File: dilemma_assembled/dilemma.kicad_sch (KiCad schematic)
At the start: 103 parts, among them J1 USB_C_Receptacle_USB2.0, J102 Serial, J103 Serial, J105 Conn_01x04_Female, J107 Conn_01x08_Female, J108 Conn_01x01_Female, J109 Conn_01x01_Female, J113 Cirque, J5 Conn_01x02, SW1 SW_Push, SW101 SW_Push, SW102 SW_Push, SW103 SW_Push, SW104 SW_Push, SW105 SW_Push, SW106 SW_Push, SW107 SW_Push, SW108 SW_Push, SW109 SW_Push, SW110 SW_SPST, SW111 SW_SPST, SW112 SW_Push, SW113 SW_Push, SW114 SW_Push, SW115 SW_Push, SW116 SW_Push, SW117 SW_Push, SW118 SW_Push, SW119 SW_Push, SW2 SW_Push, U1 RP2040, U2 GD25Q80CEIGR, U3 XC6210B332MR-G, Y1 Crystal_GND24

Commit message: add tooling holes, fancy M3 holes with vias
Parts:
- added H103, H109, H110: t, local-libraries:JLC_SMT_Assembly_Hole, symbol Mechanical:MountingHole_Pad
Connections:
- net GND: now also H103.1, H109.1, H110.1
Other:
- note added: "Assembly holes"
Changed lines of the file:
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@@
     (stroke (width 0) (type default) (color 0 0 0 0))
   )
+  (polyline (pts (xy 285.75 125.73) (xy 285.75 150.495))
+    (stroke (width 0) (type default) (color 0 0 0 0))
+  )
   (wire (pts (xy 267.97 137.16) (xy 256.54 137.16))
     (stroke (width 0) (type default) (color 0 0 0 0))
@@
     (stroke (width 0) (type default) (color 0 0 0 0))
   )
+  (polyline (pts (xy 312.42 150.495) (xy 285.75 150.495))
+    (stroke (width 0) (type default) (color 0 0 0 0))
+  )
   (wire (pts (xy 228.6 57.15) (xy 237.49 57.15))
     (stroke (width 0) (type default) (color 0 0 0 0))
@@
     (stroke (width 0) (type default) (color 0 0 0 0))
   )
+  (polyline (pts (xy 285.75 125.73) (xy 312.42 125.73))
+    (stroke (width 0) (type default) (color 0 0 0 0))
+  )
   (wire (pts (xy 90.17 228.6) (xy 93.98 228.6))
     (stroke (width 0) (type default) (color 0 0 0 0))
@@
     (stroke (width 0) (type default) (color 0 0 0 0))
   )
+  (polyline (pts (xy 312.42 125.73) (xy 312.42 150.495))
+    (stroke (width 0) (type default) (color 0 0 0 0))
+  )
   (wire (pts (xy 166.37 184.15) (xy 166.37 185.42))
     (stroke (width 0) (type default) (color 0 0 0 0))
@@
     (effects (font (size 1.778 1.778) (thickness 0.3556) bold) (justify left bottom))
   )
+  (text "Assembly holes" (at 307.34 125.73 180)
+    (effects (font (size 1.778 1.778) (thickness 0.3556) bold) (justify right bottom))
+  )
   (text "Serial" (at 249.555 165.735 0)
     (effects (font (size 1.778 1.778) (thickness 0.3556) bold) (justify left bottom))
@@
     (pin "2")
   )
+  (symbol (lib_id "power:GND") (at 306.07 135.89 0) (unit 1)
+    (in_bom yes) (on_board yes)
+    (property "Reference" "#PWR0116" (id 0) (at 306.07 142.24 0)
+      (effects (font (size 1.27 1.27)) hide)
+    )
+    (property "Value" "GND" (id 1) (at 305.914 142.8749 90)
+      (effects (font (size 1.27 1.27)) (justify left))
+    )
+    (property "Footprint" "" (id 2) (at 306.07 135.89 0)
+      (effects (font (size 1.27 1.27)) hide)
+    )
+    (property "Datasheet" "" (id 3) (at 306.07 135.89 0)
+      (effects (font (size 1.27 1.27)) hide)
+    )
+    (pin "1")
+  )
   (symbol (lib_id "Mechanical:MountingHole_Pad") (at 233.045 176.53 0) (unit 1)
     (in_bom yes) (on_board yes)
@@
     (pin "2")
   )
+  (symbol (lib_id "power:GND") (at 298.45 135.89 0) (unit 1)
+    (in_bom yes) (on_board yes)
+    (property "Reference" "#PWR0109" (id 0) (at 298.45 142.24 0)
+      (effects (font (size 1.27 1.27)) hide)
+    )
+    (property "Value" "GND" (id 1) (at 298.294 142.8749 90)
+      (effects (font (size 1.27 1.27)) (justify left))
+    )
+    (property "Footprint" "" (id 2) (at 298.45 135.89 0)
+      (effects (font (size 1.27 1.27)) hide)
+    )
+    (property "Datasheet" "" (id 3) (at 298.45 135.89 0)
+      (effects (font (size 1.27 1.27)) hide)
+    )
+    (pin "1")
+  )
   (symbol (lib_id "power:GND") (at 82.55 186.69 0) (unit 1)
     (in_bom yes) (on_board yes)
@@
     (pin "1")
   )
+  (symbol (lib_id "Mechanical:MountingHole_Pad") (at 306.07 133.35 0) (unit 1)
+    (in_bom yes) (on_board yes)
+    (property "Reference" "H110" (id 0) (at 304.8 128.27 0)
+      (effects (font (size 1.27 1.27)) (justify left))
+    )
+    (property "Value" "t" (id 1) (at 304.8 145.542 0)
+      (effects (font (size 1.27 1.27)) (justify left))
+    )
+    (property "Footprint" "local-libraries:JLC_SMT_Assembly_Hole" (id 2) (at 306.07 133.35 0)
+      (effects (font (size 1.27 1.27)) hide)
+    )
+    (property "Datasheet" "~" (id 3) (at 306.07 133.35 0)
+      (effects (font (size 1.27 1.27)) hide)
+    )
+    (pin "1")
+  )
   (symbol (lib_id "Connector:USB_C_Receptacle_USB2.0") (at 35.56 52.07 0) (unit 1)
     (in_bom yes) (on_board yes) (fields_autoplaced)
@@
     (pin "1")
   )
+  (symbol (lib_id "Mechanical:MountingHole_Pad") (at 290.83 133.35 0) (unit 1)
+    (in_bom yes) (on_board yes)
+    (property "Reference" "H103" (id 0) (at 289.56 128.27 0)
+      (effects (font (size 1.27 1.27)) (justify left))
+    )
+    (property "Value" "t" (id 1) (at 289.56 145.542 0)
+      (effects (font (size 1.27 1.27)) (justify left))
+    )
+    (property "Footprint" "local-libraries:JLC_SMT_Assembly_Hole" (id 2) (at 290.83 133.35 0)
+      (effects (font (size 1.27 1.27)) hide)
+    )
+    (property "Datasheet" "~" (id 3) (at 290.83 133.35 0)
+      (effects (font (size 1.27 1.27)) hide)
+    )
+    (pin "1")
+  )
   (symbol (lib_id "Device:C") (at 91.44 180.34 0) (unit 1)
     (in_bom yes) (on_board yes)
@@
     (pin "1")
   )
+  (symbol (lib_id "power:GND") (at 290.83 135.89 0) (unit 1)
+    (in_bom yes) (on_board yes)
+    (property "Reference" "#PWR0106" (id 0) (at 290.83 142.24 0)
+      (effects (font (size 1.27 1.27)) hide)
+    )
+    (property "Value" "GND" (id 1) (at 290.674 142.8749 90)
+      (effects (font (size 1.27 1.27)) (justify left))
+    )
+    (property "Footprint" "" (id 2) (at 290.83 135.89 0)
+      (effects (font (size 1.27 1.27)) hide)
+    )
+    (property "Datasheet" "" (id 3) (at 290.83 135.89 0)
+      (effects (font (size 1.27 1.27)) hide)
+    )
+    (pin "1")
+  )
   (symbol (lib_id "power:+3.3V") (at 299.085 103.505 0) (unit 1)
     (in_bom yes) (on_board yes)
@@
     (pin "1")
   )
+  (symbol (lib_id "Mechanical:MountingHole_Pad") (at 298.45 133.35 0) (unit 1)
+    (in_bom yes) (on_board yes)
+    (property "Reference" "H109" (id 0) (at 297.18 128.27 0)
+      (effects (font (size 1.27 1.27)) (justify left))
+    )
+    (property "Value" "t" (id 1) (at 297.18 145.542 0)
+      (effects (font (size 1.27 1.27)) (justify left))
+    )
+    (property "Footprint" "local-libraries:JLC_SMT_Assembly_Hole" (id 2) (at 298.45 133.35 0)
+      (effects (font (size 1.27 1.27)) hide)
+    )
+    (property "Datasheet" "~" (id 3) (at 298.45 133.35 0)
+      (effects (font (size 1.27 1.27)) hide)
+    )
+    (pin "1")
+  )
   (symbol (lib_id "Device:R") (at 360.045 44.45 180) (unit 1)
     (in_bom yes) (on_board yes)
@@
       (reference "#PWR0105") (unit 1) (value "+3.3V") (footprint "")
     )
+    (path "/a144bc5d-3f5b-4216-8ec6-67e8066759a2"
+      (reference "#PWR0106") (unit 1) (value "GND") (footprint "")
+    )
     (path "/d8004053-a96a-4db9-be88-aefe8064c65c"
       (reference "#PWR0107") (unit 1) (value "GND") (footprint "")
@@
       (reference "#PWR0108") (unit 1) (value "GND") (footprint "")
     )
+    (path "/47046ba4-5dc4-4560-b45c-491f19fdcef5"
+      (reference "#PWR0109") (unit 1) (value "GND") (footprint "")
+    )
     (path "/9c465d0a-3acf-44e4-926b-a8e6ae8ccd7b"
       (reference "#PWR0110") (unit 1) (value "GND") (footprint "")
@@
       (reference "#PWR0115") (unit 1) (value "+3.3V") (footprint "")
     )
+    (path "/1e9e575d-4f08-4deb-b016-bc3cb0093a0c"
+      (reference "#PWR0116") (unit 1) (value "GND") (footprint "")
+    )
     (path "/65cc9c59-39dc-4148-a69b-a97364bae0ce"
       (reference "#PWR0117") (unit 1) (value "+3.3V") (footprint "")
@@
       (reference "H102") (unit 1) (value "M4") (footprint "local-libraries:MountingHole_3mm_Pad_thin")
     )
+    (path "/6e8fbc4a-2a66-4de2-9627-0a21b2e2f627"
+      (reference "H103") (unit 1) (value "t") (footprint "local-libraries:JLC_SMT_Assembly_Hole")
+    )
     (path "/b3d2b3b2-eee3-4354-96ae-35ebc3a7e3fd"
       (reference "H104") (unit 1) (value "M4") (footprint "local-libraries:MountingHole_3mm_Pad_thin")
@@
       (reference "H108") (unit 1) (value "M4") (footprint "local-libraries:MountingHole_3mm_Pad_thin")
     )
+    (path "/bd7d1550-12f2-4e61-8301-dc127a990905"
+      (reference "H109") (unit 1) (value "t") (footprint "local-libraries:JLC_SMT_Assembly_Hole")
+    )
+    (path "/5ccba51b-82b7-45cf-91ae-52778ba511ad"
+      (reference "H110") (unit 1) (value "t") (footprint "local-libraries:JLC_SMT_Assembly_Hole")
+    )
     (path "/6125bb34-31fe-49ed-b2ab-61dab24d450a"

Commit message: add back mouse bites
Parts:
- H101, H102, H104, H105, H106, H107, H108: footprint local-libraries:MountingHole_3mm_Pad_thin -> local-libraries:MountingHole_3mm_Pad_Via
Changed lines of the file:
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@@
       (effects (font (size 1.27 1.27)) (justify left))
     )
-    (property "Footprint" "local-libraries:MountingHole_3mm_Pad_thin" (id 2) (at 233.045 176.53 0)
+    (property "Footprint" "local-libraries:MountingHole_3mm_Pad_Via" (id 2) (at 233.045 176.53 0)
       (effects (font (size 1.27 1.27)) hide)
     )
@@
       (effects (font (size 1.27 1.27)) (justify left))
     )
-    (property "Footprint" "local-libraries:MountingHole_3mm_Pad_thin" (id 2) (at 184.15 176.53 0)
+    (property "Footprint" "local-libraries:MountingHole_3mm_Pad_Via" (id 2) (at 184.15 176.53 0)
       (effects (font (size 1.27 1.27)) hide)
     )
@@
       (effects (font (size 1.27 1.27)) (justify left))
     )
-    (property "Footprint" "local-libraries:MountingHole_3mm_Pad_thin" (id 2) (at 226.695 176.53 0)
+    (property "Footprint" "local-libraries:MountingHole_3mm_Pad_Via" (id 2) (at 226.695 176.53 0)
       (effects (font (size 1.27 1.27)) hide)
     )
@@
       (effects (font (size 1.27 1.27)) (justify left))
     )
-    (property "Footprint" "local-libraries:MountingHole_3mm_Pad_thin" (id 2) (at 190.5 176.53 0)
+    (property "Footprint" "local-libraries:MountingHole_3mm_Pad_Via" (id 2) (at 190.5 176.53 0)
       (effects (font (size 1.27 1.27)) hide)
     )
@@
       (effects (font (size 1.27 1.27)) (justify left))
     )
-    (property "Footprint" "local-libraries:MountingHole_3mm_Pad_thin" (id 2) (at 239.395 176.53 0)
+    (property "Footprint" "local-libraries:MountingHole_3mm_Pad_Via" (id 2) (at 239.395 176.53 0)
       (effects (font (size 1.27 1.27)) hide)
     )
@@
       (effects (font (size 1.27 1.27)) (justify left))
     )
-    (property "Footprint" "local-libraries:MountingHole_3mm_Pad_thin" (id 2) (at 209.55 176.53 0)
+    (property "Footprint" "local-libraries:MountingHole_3mm_Pad_Via" (id 2) (at 209.55 176.53 0)
       (effects (font (size 1.27 1.27)) hide)
     )
@@
       (effects (font (size 1.27 1.27)) (justify left))
     )
-    (property "Footprint" "local-libraries:MountingHole_3mm_Pad_thin" (id 2) (at 220.345 176.53 0)
+    (property "Footprint" "local-libraries:MountingHole_3mm_Pad_Via" (id 2) (at 220.345 176.53 0)
       (effects (font (size 1.27 1.27)) hide)
     )
@@
     )
     (path "/2f4248fc-bac1-4746-8fce-b7d7e338527c"
-      (reference "H101") (unit 1) (value "M4") (footprint "local-libraries:MountingHole_3mm_Pad_thin")
+      (reference "H101") (unit 1) (value "M4") (footprint "local-libraries:MountingHole_3mm_Pad_Via")
     )
     (path "/9cb3ab70-f859-494a-87ac-434fbc66c33e"
-      (reference "H102") (unit 1) (value "M4") (footprint "local-libraries:MountingHole_3mm_Pad_thin")
+      (reference "H102") (unit 1) (value "M4") (footprint "local-libraries:MountingHole_3mm_Pad_Via")
     )
     (path "/6e8fbc4a-2a66-4de2-9627-0a21b2e2f627"
@@
     )
     (path "/b3d2b3b2-eee3-4354-96ae-35ebc3a7e3fd"
-      (reference "H104") (unit 1) (value "M4") (footprint "local-libraries:MountingHole_3mm_Pad_thin")
+      (reference "H104") (unit 1) (value "M4") (footprint "local-libraries:MountingHole_3mm_Pad_Via")
     )
     (path "/f149694e-4336-45f7-8a0b-aed91118ad18"
-      (reference "H105") (unit 1) (value "M4") (footprint "local-libraries:MountingHole_3mm_Pad_thin")
+      (reference "H105") (unit 1) (value "M4") (footprint "local-libraries:MountingHole_3mm_Pad_Via")
     )
     (path "/4caa68da-1d74-422f-8bbe-3c28c9ea4b69"
-      (reference "H106") (unit 1) (value "M4") (footprint "local-libraries:MountingHole_3mm_Pad_thin")
+      (reference "H106") (unit 1) (value "M4") (footprint "local-libraries:MountingHole_3mm_Pad_Via")
     )
     (path "/1ebf55b2-09a7-4dc8-8b62-2c2166fb1446"
-      (reference "H107") (unit 1) (value "M4") (footprint "local-libraries:MountingHole_3mm_Pad_thin")
+      (reference "H107") (unit 1) (value "M4") (footprint "local-libraries:MountingHole_3mm_Pad_Via")
     )
     (path "/afadc09f-0628-42ff-b630-9cf4ae0a8b3f"
-      (reference "H108") (unit 1) (value "M4") (footprint "local-libraries:MountingHole_3mm_Pad_thin")
+      (reference "H108") (unit 1) (value "M4") (footprint "local-libraries:MountingHole_3mm_Pad_Via")
     )
     (path "/bd7d1550-12f2-4e61-8301-dc127a990905"

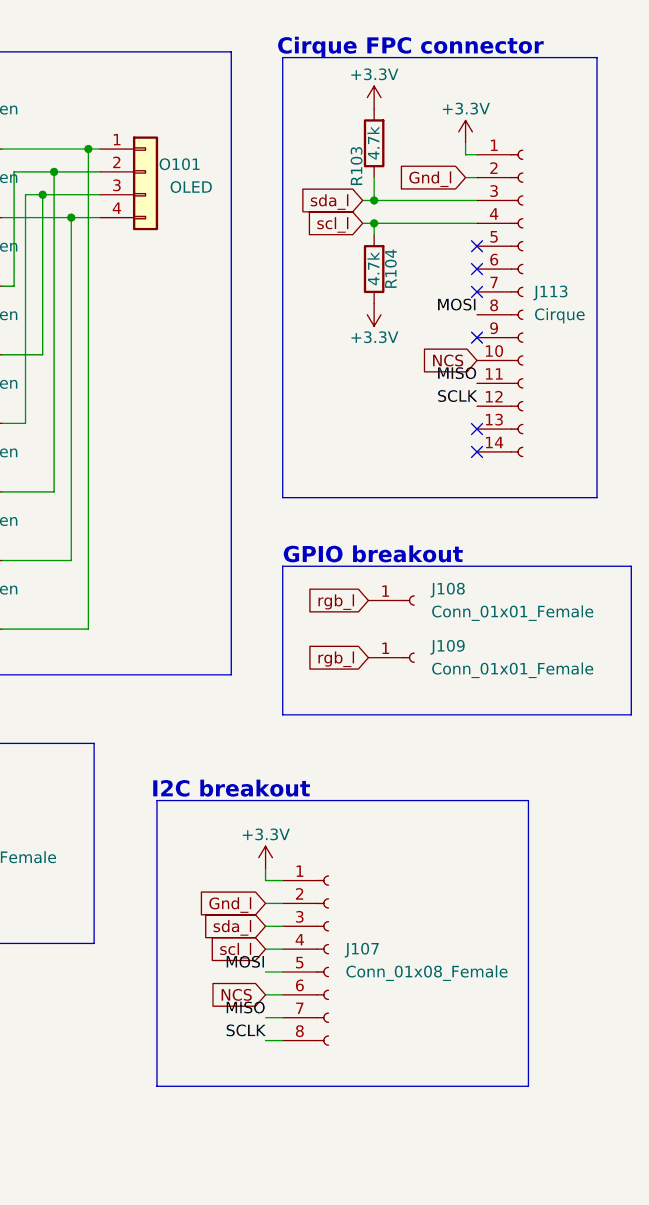
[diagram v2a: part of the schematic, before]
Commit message: switch up fpc connections
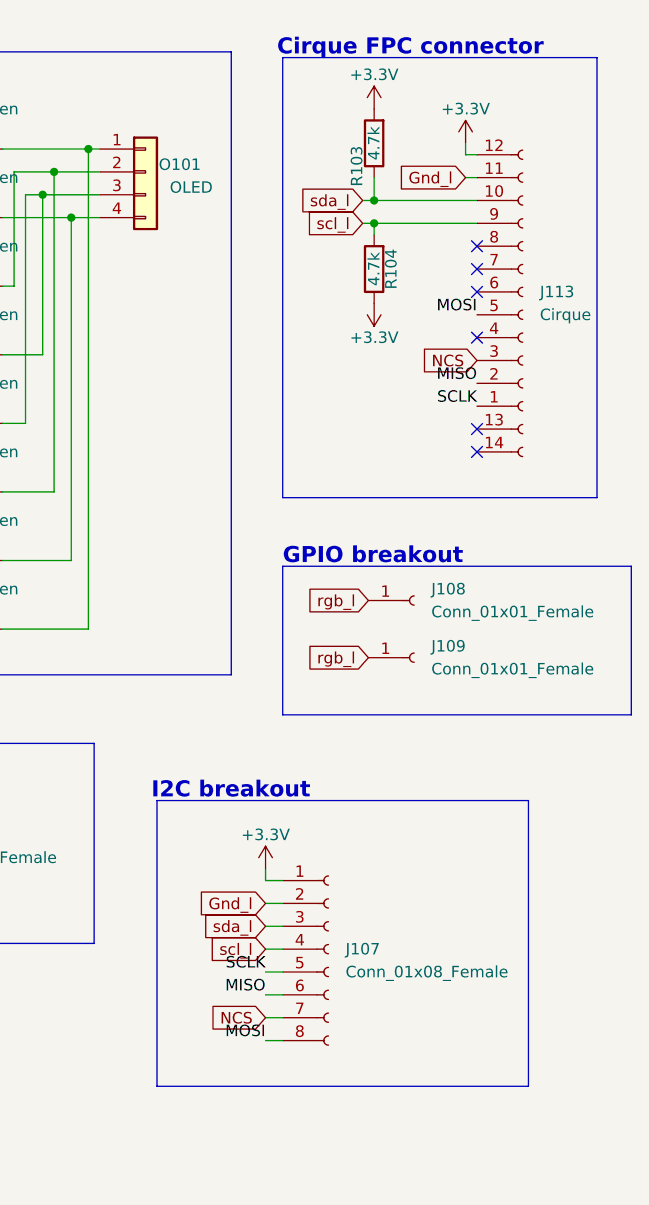
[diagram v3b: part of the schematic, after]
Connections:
- net +3V3: now also J113.12 (Pin_12); no longer J113.1 (Pin_1)
- net GND: now also J113.11 (Pin_11); no longer J113.2 (Pin_2)
- net NCS: now also J107.7 (Pin_7), J113.3 (Pin_3); no longer J107.6 (Pin_6), J113.10 (Pin_10)
- net miso_l: now also J107.6 (Pin_6), J113.2 (Pin_2); no longer J107.7 (Pin_7), J113.11 (Pin_11)
- net mosi_l: now also J107.8 (Pin_8), J113.5 (Pin_5); no longer J107.5 (Pin_5), J113.8 (Pin_8)
- net sc_l: now also J107.5 (Pin_5), J113.1 (Pin_1); no longer J107.8 (Pin_8), J113.12 (Pin_12)
- net scl_l: now also J113.9 (Pin_9); no longer J113.4 (Pin_4)
- net sda_l: now also J113.10 (Pin_10); no longer J113.3 (Pin_3)
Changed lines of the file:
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@@
     (effects (font (size 1.27 1.27)) (justify right bottom))
   )
-  (label "MOSI" (at 347.98 122.555 180)
+  (label "MOSI" (at 347.98 130.175 180)
     (effects (font (size 1.27 1.27)) (justify right bottom))
   )
@@
     (effects (font (size 1.27 1.27)) (justify right bottom))
   )
-  (label "SCLK" (at 347.98 130.175 180)
+  (label "SCLK" (at 347.98 122.555 180)
     (effects (font (size 1.27 1.27)) (justify right bottom))
   )
@@
     (effects (font (size 1.27 1.27)) (justify right bottom))
   )
-  (label "MISO" (at 347.98 127.635 180)
+  (label "MISO" (at 347.98 125.095 180)
     (effects (font (size 1.27 1.27)) (justify right bottom))
   )
@@
     )
   )
-  (global_label "NCS" (shape input) (at 347.98 125.095 180)
+  (global_label "NCS" (shape input) (at 347.98 127.635 180)
     (effects (font (size 1.27 1.27)) (justify right))
-    (property "Intersheet References" "${INTERSHEET_REFS}" (id 0) (at 343.5107 125.0156 0)
+    (property "Intersheet References" "${INTERSHEET_REFS}" (id 0) (at 343.5107 127.5556 0)
       (effects (font (size 1.27 1.27)) (justify right) hide)
     )
@@
   (symbol (lib_id "Connector:Conn_01x14_Female") (at 376.555 46.99 0) (unit 1)
     (in_bom yes) (on_board yes) (fields_autoplaced)
-    (property "Reference" "J113" (id 0) (at 377.825 46.9899 0)
+    (property "Reference" "J113" (id 0) (at 378.46 46.9899 0)
       (effects (font (size 1.27 1.27)) (justify left))
     )
-    (property "Value" "Cirque" (id 1) (at 377.825 49.5299 0)
+    (property "Value" "Cirque" (id 1) (at 378.46 49.5299 0)
       (effects (font (size 1.27 1.27)) (justify left))
     )
-    (property "Footprint" "local-libraries:FPC-SMD_FPC05012-09200-.5mm" (id 2) (at 376.555 46.99 0)
+    (property "Footprint" "local-libraries:FPC-SMD_FPC05012-09200-.5mm" (id 2) (at 398.145 43.18 0)
       (effects (font (size 1.27 1.27)) hide)
     )
@@
       (effects (font (size 1.27 1.27)) hide)
     )
-    (pin "1")
+    (pin "14")
+    (pin "8")
+    (pin "9")
     (pin "10")
     (pin "11")
     (pin "12")
     (pin "13")
-    (pin "14")
+    (pin "1")
     (pin "2")
     (pin "3")
@@
     (pin "6")
     (pin "7")
-    (pin "8")
-    (pin "9")
   )
   (symbol (lib_id "Mechanical:MountingHole_Pad") (at 220.345 176.53 0) (unit 1)
